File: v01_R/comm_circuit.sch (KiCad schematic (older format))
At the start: 16 parts, among them J1 USB, Q1 MOSFET_N, Q2 MOSFET_N, U3 FT232RL

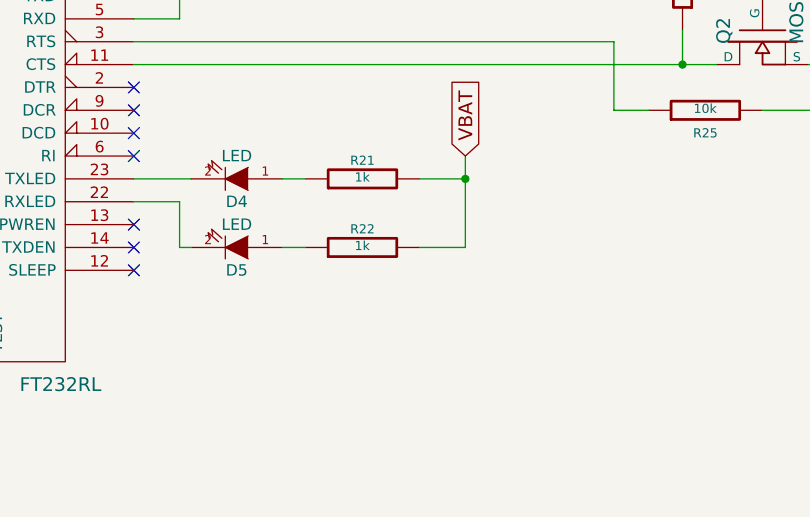
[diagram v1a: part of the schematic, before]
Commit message: Updating entire schematic and footprint selections. Adding jst-ph footprints.
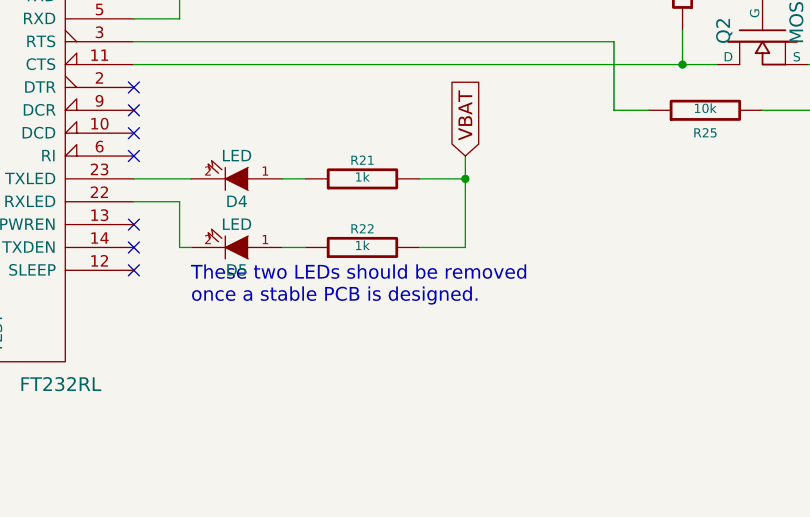
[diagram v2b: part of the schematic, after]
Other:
- note added: "These two LEDs should be removed \nonce a stable PCB is designed."
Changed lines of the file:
@@
 Sheet 3 4
 Title ""
-Date "16 jan 2015"
+Date "17 jan 2015"
 Rev ""
 Comp ""
@@
 $EndComp
 $Comp
-L GND #PWR08
+L GND #PWR07
 U 1 1 541E1178
 P 2550 3500
-F 0 "#PWR08" H 2550 3500 30  0001 C CNN
+F 0 "#PWR07" H 2550 3500 30  0001 C CNN
 F 1 "GND" H 2550 3430 30  0001 C CNN
 F 2 "" H 2550 3500 60  0000 C CNN
@@
 NoConn ~ 4350 2600
 $Comp
-L GND #PWR09
+L GND #PWR08
 U 1 1 541E1245
 P 5300 4800
-F 0 "#PWR09" H 5300 4800 30  0001 C CNN
+F 0 "#PWR08" H 5300 4800 30  0001 C CNN
 F 1 "GND" H 5300 4730 30  0001 C CNN
 F 2 "" H 5300 4800 60  0000 C CNN
@@
 $EndComp
 $Comp
-L GND #PWR010
+L GND #PWR09
 U 1 1 541E14B3
 P 2300 3500
-F 0 "#PWR010" H 2300 3500 30  0001 C CNN
+F 0 "#PWR09" H 2300 3500 30  0001 C CNN
 F 1 "GND" H 2300 3430 30  0001 C CNN
 F 2 "" H 2300 3500 60  0000 C CNN
@@
 $EndComp
 $Comp
-L GND #PWR011
+L GND #PWR010
 U 1 1 541E14BA
 P 2050 3500
-F 0 "#PWR011" H 2050 3500 30  0001 C CNN
+F 0 "#PWR010" H 2050 3500 30  0001 C CNN
 F 1 "GND" H 2050 3430 30  0001 C CNN
 F 2 "" H 2050 3500 60  0000 C CNN
@@
 	1    0    0    -1
 $EndComp
-NoConn ~ 4350 3350
 NoConn ~ 4350 3550
 NoConn ~ 4350 3650
@@
 Connection ~ 7650 3450
 $Comp
-L +5V #PWR012
+L +5V #PWR011
 U 1 1 5439D737
 P 2750 2650
-F 0 "#PWR012" H 2750 2740 20  0001 C CNN
+F 0 "#PWR011" H 2750 2740 20  0001 C CNN
 F 1 "+5V" H 2750 2740 30  0000 C CNN
 F 2 "" H 2750 2650 60  0000 C CNN
@@
 Connection ~ 4150 2200
 NoConn ~ 4350 3850
+Text Notes 6450 4000 0    60   ~ 0
+These two LEDs should be removed \nonce a stable PCB is designed.
+NoConn ~ 4350 3350
 $EndSCHEMATC

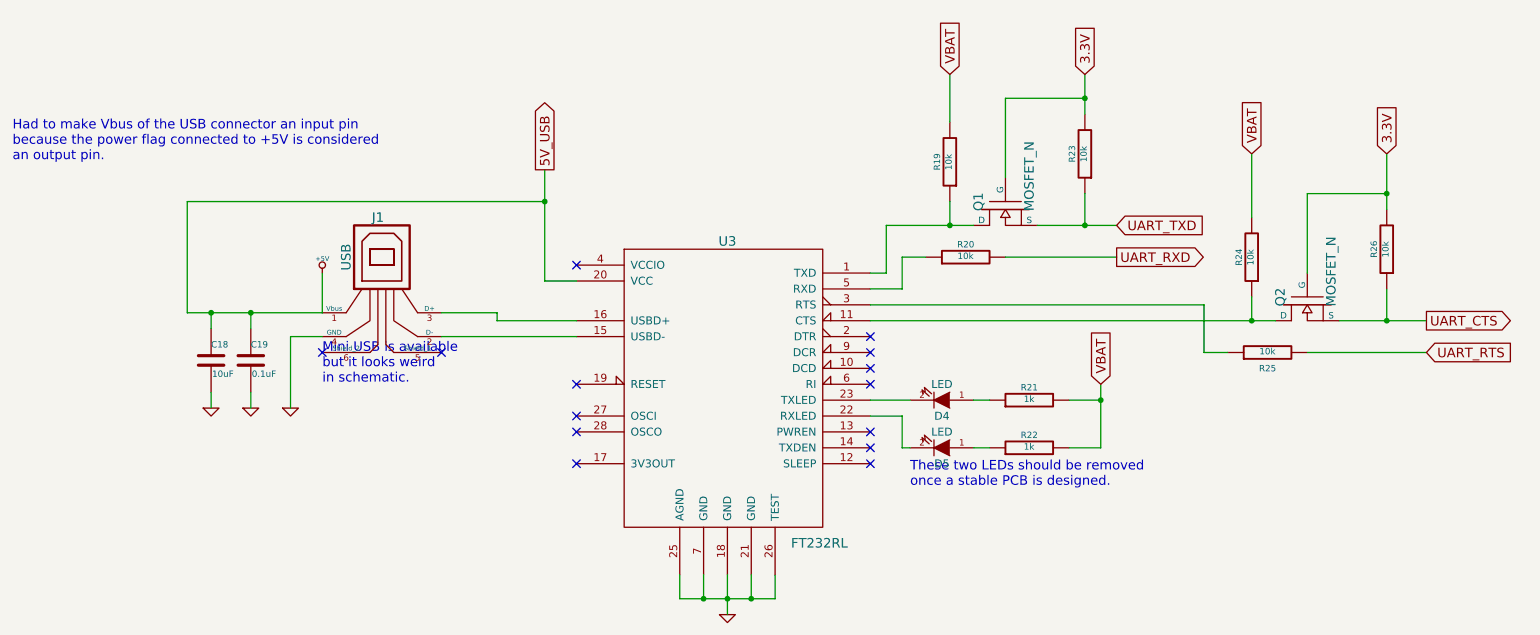
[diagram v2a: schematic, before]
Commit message: Adding very rough initial version of PCB. The BA driver pads were not exact yet (based off of a Sonion driver datasheet).
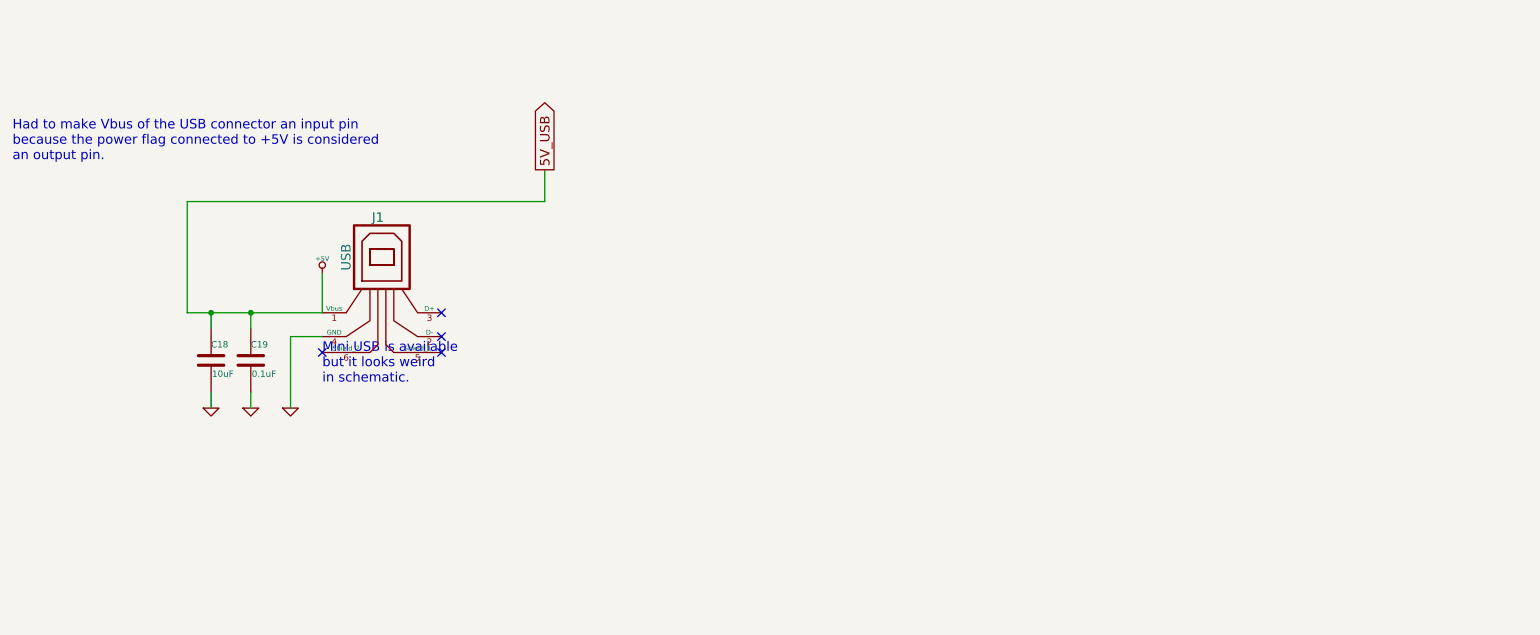
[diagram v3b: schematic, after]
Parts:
- removed D4, D5: LED, ~, symbol LED
- removed Q1, Q2: MOSFET_N, ~, symbol MOSFET_N
- removed R19, R20, R23, R24, R25, R26: 10k, ~, symbol R
- removed R21, R22: 1k, ~, symbol R
- removed U3: FT232RL, symbol FT232RL
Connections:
- no-connect marks 14 -> 4
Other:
- note removed: "These two LEDs should be removed \nonce a stable PCB is designed."
